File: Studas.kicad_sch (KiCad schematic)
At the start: 50 parts, among them J1 MJ-4PP-9, J2 MJ-4PP-9, SW10_L1 SW_Diode_Combined, SW10_R1 SW_Diode_Combined, SW11_L1 SW_Diode_Combined, SW11_R1 SW_Diode_Combined, SW12_L1 SW_Diode_Combined, SW12_R1 SW_Diode_Combined, SW13_L1 SW_Diode_Combined, SW13_R1 SW_Diode_Combined, SW14_L1 SW_Diode_Combined, SW14_R1 SW_Diode_Combined, SW15_L1 SW_Diode_Combined, SW15_R1 SW_Diode_Combined, SW16_L1 SW_Diode_Combined, SW16_R1 SW_Diode_Combined, SW17_L1 SW_Diode_Combined, SW17_R1 SW_Diode_Combined, SW1_L1 SW_Diode_Combined, SW1_R1 SW_Diode_Combined, SW2_L1 SW_Diode_Combined, SW2_R1 SW_Diode_Combined, SW3_L1 SW_Diode_Combined, SW3_R1 SW_Diode_Combined, SW4_L1 SW_Diode_Combined, SW4_R1 SW_Diode_Combined, SW5_L1 SW_Diode_Combined, SW5_R1 SW_Diode_Combined, SW6_L1 SW_Diode_Combined, SW6_R1 SW_Diode_Combined, SW7_L1 SW_Diode_Combined, SW7_R1 SW_Diode_Combined, SW8_L1 SW_Diode_Combined, SW8_R1 SW_Diode_Combined, SW9_L1 SW_Diode_Combined, SW9_R1 SW_Diode_Combined, U1 xiao-ble, U2 xiao-ble

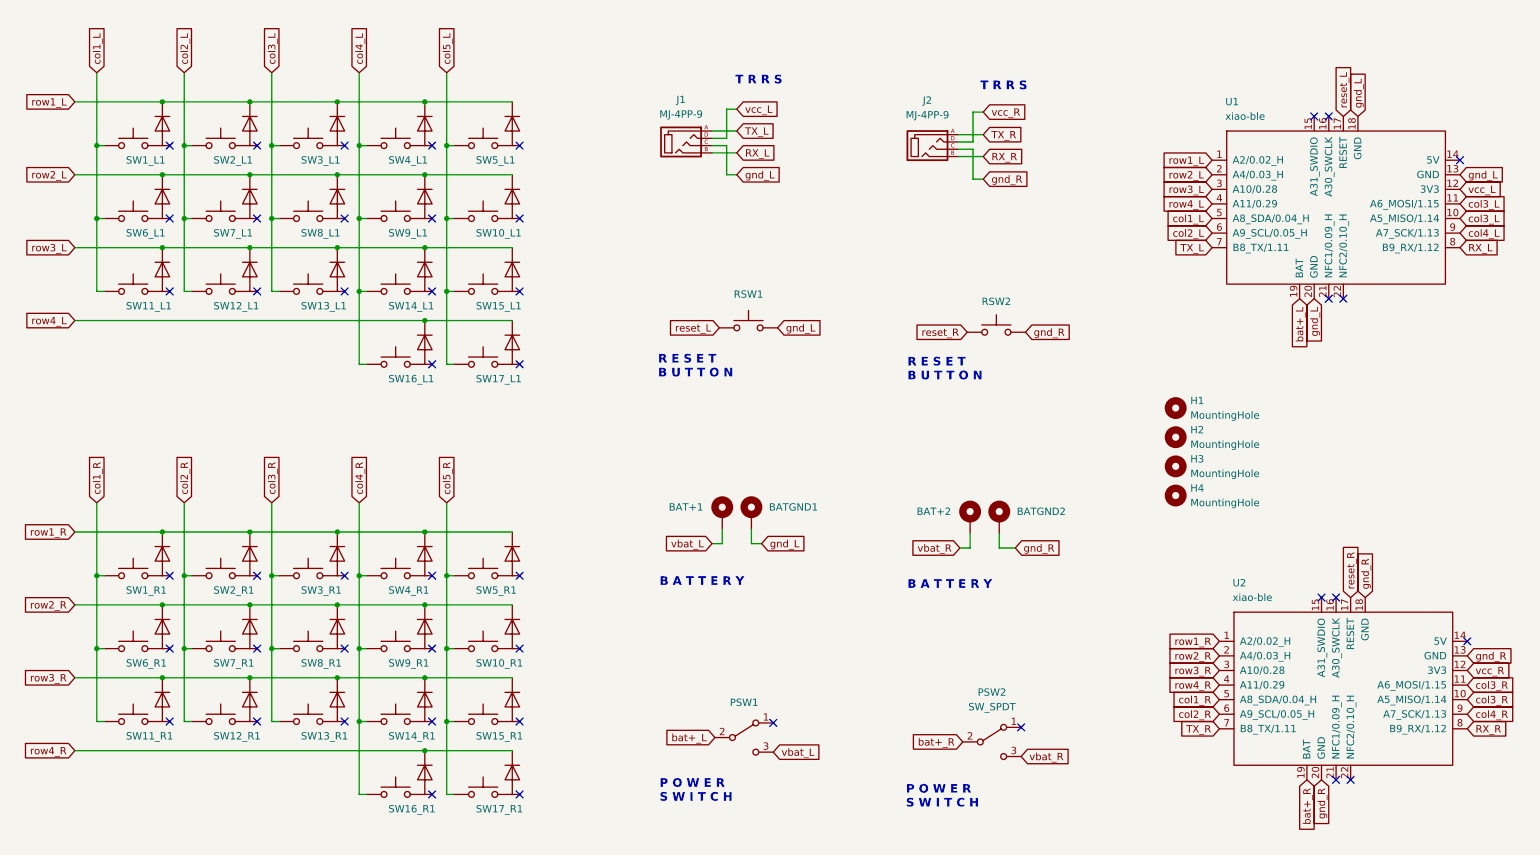
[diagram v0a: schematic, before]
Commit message: Finished Routing - Ready to order
I FINALLY ROUTED THE BOARD :)

Added EVERY symbol/footprint used in the project.

There are some footprint warnings that I couldn't care less.

Suggestions for V1.2:

- Make Switch plate board 
- Add some teardrop pads
- Make copper traces "melt" (using round track plugin)
- Check for better placement of mounting holes
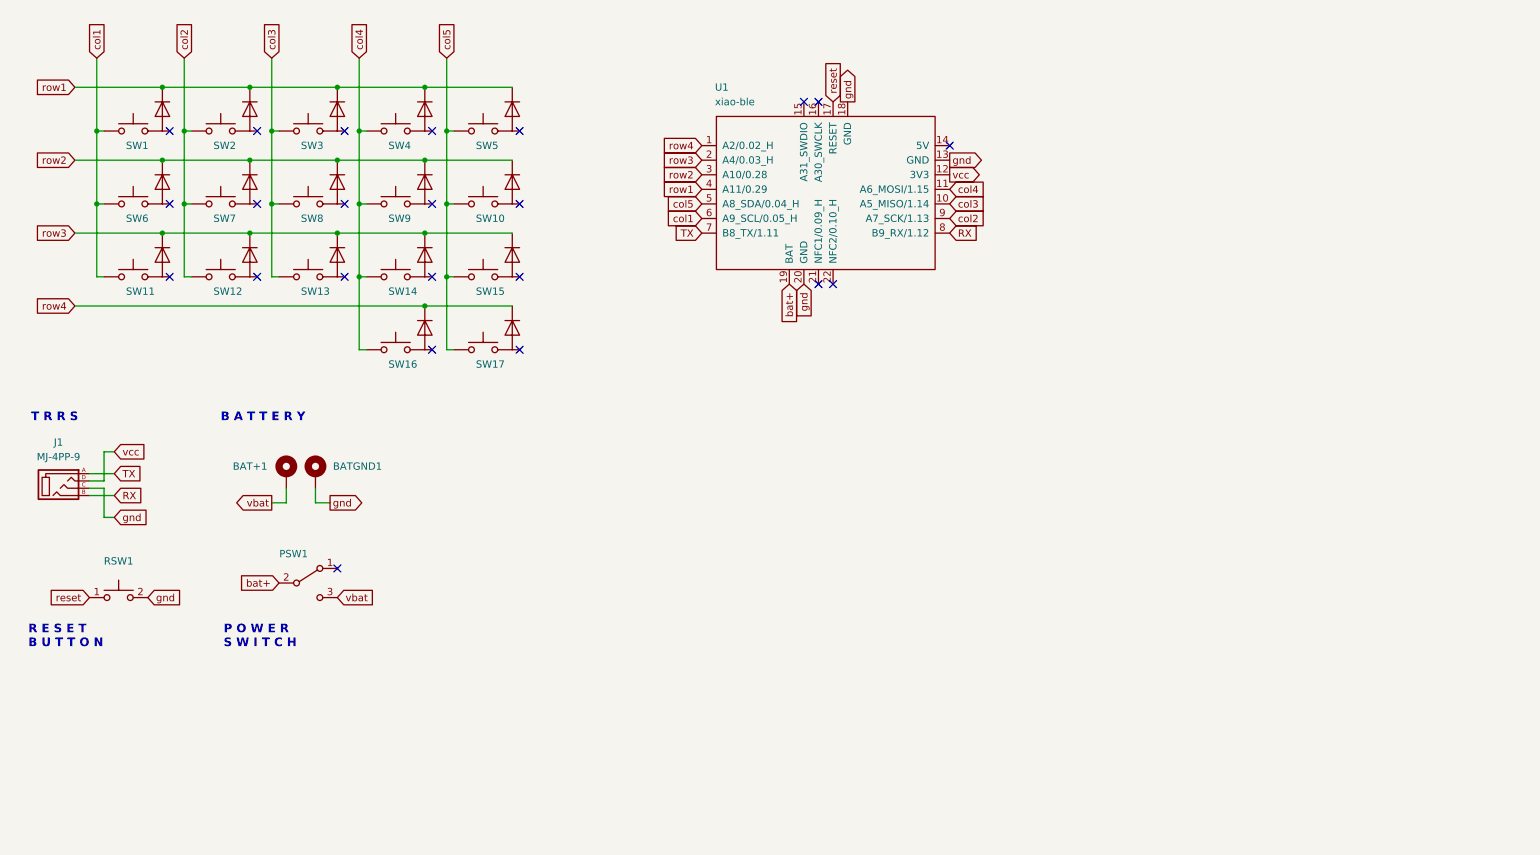
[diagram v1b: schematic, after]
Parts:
- removed BAT+2: +, TOTEMlib:BatteryPad, symbol Mechanical:MountingHole_Pad
- removed BATGND2: -, TOTEMlib:BatteryPad, symbol Mechanical:MountingHole_Pad
- removed H1, H2, H3, H4: MountingHole, MountingHole:MountingHole_2.2mm_M2_Pad_Via, symbol Mechanical:MountingHole
- removed J2: MJ-4PP-9, TOTEMlib:MJ-4PP-9_1side, symbol kbd:MJ-4PP-9
- removed PSW2: SW_SPDT, TOTEMlib:MSK12C02, symbol Switch:SW_SPDT
- removed RSW2: SW_Push, TOTEMlib:SKHLLCA010, symbol Switch:SW_Push
- removed SW10_R1, SW12_R1, SW13_R1, SW14_R1, SW15_R1, SW16_R1, SW17_R1, SW1_R1, SW2_R1, SW3_R1, SW4_R1, SW5_R1, SW6_R1, SW7_R1, SW8_R1, SW9_R1: SW_Diode_Combined, dotleon:SW_MX_GATLP_CHOC_reversible, symbol dotleon:SW_Diode_Combined
- removed SW11_R1: SW_Diode_Combined, dotleon:SW_MX_GATLP_CHOC_reversible_sideofpcb, symbol dotleon:SW_Diode_Combined
- removed U2: xiao-ble, TOTEMlib:xiao-ble-smd-cutout, symbol mcu:xiao-ble
- BAT+1, BATGND1: footprint TOTEMlib:BatteryPad -> STUDASlib:BatteryPad; symbol Mechanical:MountingHole_Pad -> Studaskeeb:MountingHole_Pad
- J1: footprint TOTEMlib:MJ-4PP-9_1side -> STUDASlib:MJ-4PP-9_1side; symbol kbd:MJ-4PP-9 -> Studaskeeb:MJ-4PP-9
- PSW1: footprint TOTEMlib:MSK12C02 -> STUDASlib:MSK12C02; symbol Switch:SW_SPDT -> Studaskeeb:SW_SPDT
- RSW1: footprint TOTEMlib:SKHLLCA010 -> STUDASlib:SKHLLCA010
- SW1: renamed from SW1_L1; footprint dotleon:SW_MX_GATLP_CHOC_reversible -> STUDASlib:SW_MX_GATLP_CHOC_reversible; symbol dotleon:SW_Diode_Combined -> Studaskeeb:SW_Diode_Combined_16
- SW10: renamed from SW10_L1; footprint dotleon:SW_MX_GATLP_CHOC_reversible -> STUDASlib:SW_MX_GATLP_CHOC_reversible; symbol dotleon:SW_Diode_Combined -> Studaskeeb:SW_Diode_Combined_16
- SW11: renamed from SW11_L1; footprint dotleon:SW_MX_GATLP_CHOC_reversible_sideofpcb -> STUDASlib:SW_MX_GATLP_CHOC_reversible; symbol dotleon:SW_Diode_Combined -> Studaskeeb:SW_Diode_Combined_16
- SW12: renamed from SW12_L1; footprint dotleon:SW_MX_GATLP_CHOC_reversible -> STUDASlib:SW_MX_GATLP_CHOC_reversible; symbol dotleon:SW_Diode_Combined -> Studaskeeb:SW_Diode_Combined_16
- SW13: renamed from SW13_L1; footprint dotleon:SW_MX_GATLP_CHOC_reversible -> STUDASlib:SW_MX_GATLP_CHOC_reversible; symbol dotleon:SW_Diode_Combined -> Studaskeeb:SW_Diode_Combined_16
- SW14: renamed from SW14_L1; footprint dotleon:SW_MX_GATLP_CHOC_reversible -> STUDASlib:SW_MX_GATLP_CHOC_reversible; symbol dotleon:SW_Diode_Combined -> Studaskeeb:SW_Diode_Combined_16
- SW15: renamed from SW15_L1; footprint dotleon:SW_MX_GATLP_CHOC_reversible -> STUDASlib:SW_MX_GATLP_CHOC_reversible; symbol dotleon:SW_Diode_Combined -> Studaskeeb:SW_Diode_Combined_16
- SW16: renamed from SW16_L1; footprint dotleon:SW_MX_GATLP_CHOC_reversible -> STUDASlib:SW_MX_GATLP_CHOC_reversible; symbol dotleon:SW_Diode_Combined -> Studaskeeb:SW_Diode_Combined_16
- SW17: renamed from SW17_L1; footprint dotleon:SW_MX_GATLP_CHOC_reversible -> STUDASlib:SW_MX_GATLP_CHOC_reversible; symbol dotleon:SW_Diode_Combined -> Studaskeeb:SW_Diode_Combined_16
- SW2: renamed from SW2_L1; footprint dotleon:SW_MX_GATLP_CHOC_reversible -> STUDASlib:SW_MX_GATLP_CHOC_reversible; symbol dotleon:SW_Diode_Combined -> Studaskeeb:SW_Diode_Combined_16
- SW3: renamed from SW3_L1; footprint dotleon:SW_MX_GATLP_CHOC_reversible -> STUDASlib:SW_MX_GATLP_CHOC_reversible; symbol dotleon:SW_Diode_Combined -> Studaskeeb:SW_Diode_Combined_16
- SW4: renamed from SW4_L1; footprint dotleon:SW_MX_GATLP_CHOC_reversible -> STUDASlib:SW_MX_GATLP_CHOC_reversible; symbol dotleon:SW_Diode_Combined -> Studaskeeb:SW_Diode_Combined_16
- SW5: renamed from SW5_L1; footprint dotleon:SW_MX_GATLP_CHOC_reversible -> STUDASlib:SW_MX_GATLP_CHOC_reversible; symbol dotleon:SW_Diode_Combined -> Studaskeeb:SW_Diode_Combined_16
- SW6: renamed from SW6_L1; footprint dotleon:SW_MX_GATLP_CHOC_reversible -> STUDASlib:SW_MX_GATLP_CHOC_reversible; symbol dotleon:SW_Diode_Combined -> Studaskeeb:SW_Diode_Combined_16
- SW7: renamed from SW7_L1; footprint dotleon:SW_MX_GATLP_CHOC_reversible -> STUDASlib:SW_MX_GATLP_CHOC_reversible; symbol dotleon:SW_Diode_Combined -> Studaskeeb:SW_Diode_Combined_16
- SW8: renamed from SW8_L1; footprint dotleon:SW_MX_GATLP_CHOC_reversible -> STUDASlib:SW_MX_GATLP_CHOC_reversible; symbol dotleon:SW_Diode_Combined -> Studaskeeb:SW_Diode_Combined_16
- SW9: renamed from SW9_L1; footprint dotleon:SW_MX_GATLP_CHOC_reversible -> STUDASlib:SW_MX_GATLP_CHOC_reversible; symbol dotleon:SW_Diode_Combined -> Studaskeeb:SW_Diode_Combined_16
- U1: footprint TOTEMlib:xiao-ble-smd-cutout -> STUDASlib:xiao-ble-smd-cutout; symbol mcu:xiao-ble -> Studaskeeb:xiao-ble
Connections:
- net RX_L renamed RX
- net TX_L renamed TX
- net bat+_L renamed bat+
- net col1_L renamed col1
- net col1: now also U1.6 (A9_SCL/0.05_H); no longer U1.5 (A8_SDA/0.04_H)
- net col2_L renamed col2
- net col2: now also U1.9 (A7_SCK/1.13); no longer U1.6 (A9_SCL/0.05_H)
- net col3_L renamed col3
- net col3: no longer U1.11 (A6_MOSI/1.15)
- net col4_L renamed col4
- net col4: now also U1.11 (A6_MOSI/1.15); no longer U1.9 (A7_SCK/1.13)
- net col5_L renamed col5
- net col5: now also U1.5 (A8_SDA/0.04_H)
- net gnd_L renamed gnd
- net reset_L renamed reset
- net row1_L renamed row1
- net row1: now also U1.4 (A11/0.29); no longer U1.1 (A2/0.02_H)
- net row2_L renamed row2
- net row2: now also U1.3 (A10/0.28); no longer U1.2 (A4/0.03_H)
- net row3_L renamed row3
- net row3: now also U1.2 (A4/0.03_H); no longer U1.3 (A10/0.28)
- net row4_L renamed row4
- net row4: now also U1.1 (A2/0.02_H); no longer U1.4 (A11/0.29)
- net vbat_L renamed vbat
- net vcc_L renamed vcc
- no-connect marks 46 -> 23
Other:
- moved on the sheet: BAT+1, BATGND1, J1, PSW1, SW1, SW10, SW11, SW12, SW13, SW14, SW15, SW16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
